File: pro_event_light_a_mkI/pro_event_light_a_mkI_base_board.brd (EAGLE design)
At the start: 68.9 x 76.6 mm, 85 parts, among them K1 62201021121, SW1 ALPS_EC11D

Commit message: modelled all four IL4001 PMICs
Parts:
- moved PMIC5:U1 276.1 mm to (59.9, 11.9), turned to 90 degrees
- moved PMIC5:R14 273.4 mm to (59.2, 9.78)
- moved PMIC5:PMIC1 269.8 mm to (56.8, 13.2), turned to 270 degrees
- moved PMIC5:L2 267.0 mm to (63.9, 11.8), turned to 180 degrees
- moved PMIC5:DZ1 262.9 mm to (61.0, 15.7), turned to 270 degrees
- moved PMIC5:C8 257.6 mm to (56.0, 15.7), turned to 180 degrees
- moved PMIC4:U1 248.0 mm to (42.8, 20.8), turned to 90 degrees
- moved PMIC4:R14 245.0 mm to (41.7, 18.0)
- moved PMIC4:PMIC1 242.1 mm to (39.4, 22.1), turned to 270 degrees
- moved PMIC3:U1 239.2 mm to (59.6, 26.8), turned to 90 degrees
- moved PMIC4:L2 238.3 mm to (47.0, 20.3), turned to 180 degrees
- moved PMIC3:R14 236.6 mm to (58.5, 24.5)
- moved PMIC4:DZ1 235.3 mm to (43.2, 24.8), turned to 270 degrees
- moved PMIC3:PMIC1 233.1 mm to (55.9, 28.2), turned to 270 degrees
- moved PMIC3:L2 230.5 mm to (64.0, 27.2), turned to 180 degrees
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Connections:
- removed net PMIC3:PMIC_IL4001_S24V: PMIC3:C8.2, PMIC3:DZ1.C, PMIC3:PMIC1.1
- removed net PMIC4:PMIC_IL4001_GND: PMIC4:C8.1, PMIC4:PMIC1.2, PMIC4:PMIC1.5, PMIC4:R14.1, PMIC4:U1.2
- net GND_MCU: now also PMIC4:C8.1, PMIC4:PMIC1.2, PMIC4:PMIC1.5, PMIC4:R14.1, PMIC4:U1.2
- net SUPPLY_24V: now also PMIC3:C8.2, PMIC3:DZ1.C, PMIC3:PMIC1.1
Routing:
- net PMIC4:N$2: track 0.00 -> 5.44 mm
- net PMIC3:N$2: track 0.00 -> 5.05 mm
- net PMIC5:N$2: track 0.00 -> 4.65 mm
- added copper zone on layer 1, net PMIC3:N$29
- added copper zone on layer 1, net PMIC4:N$29
- added copper zone on layer 1, net PMIC5:N$29

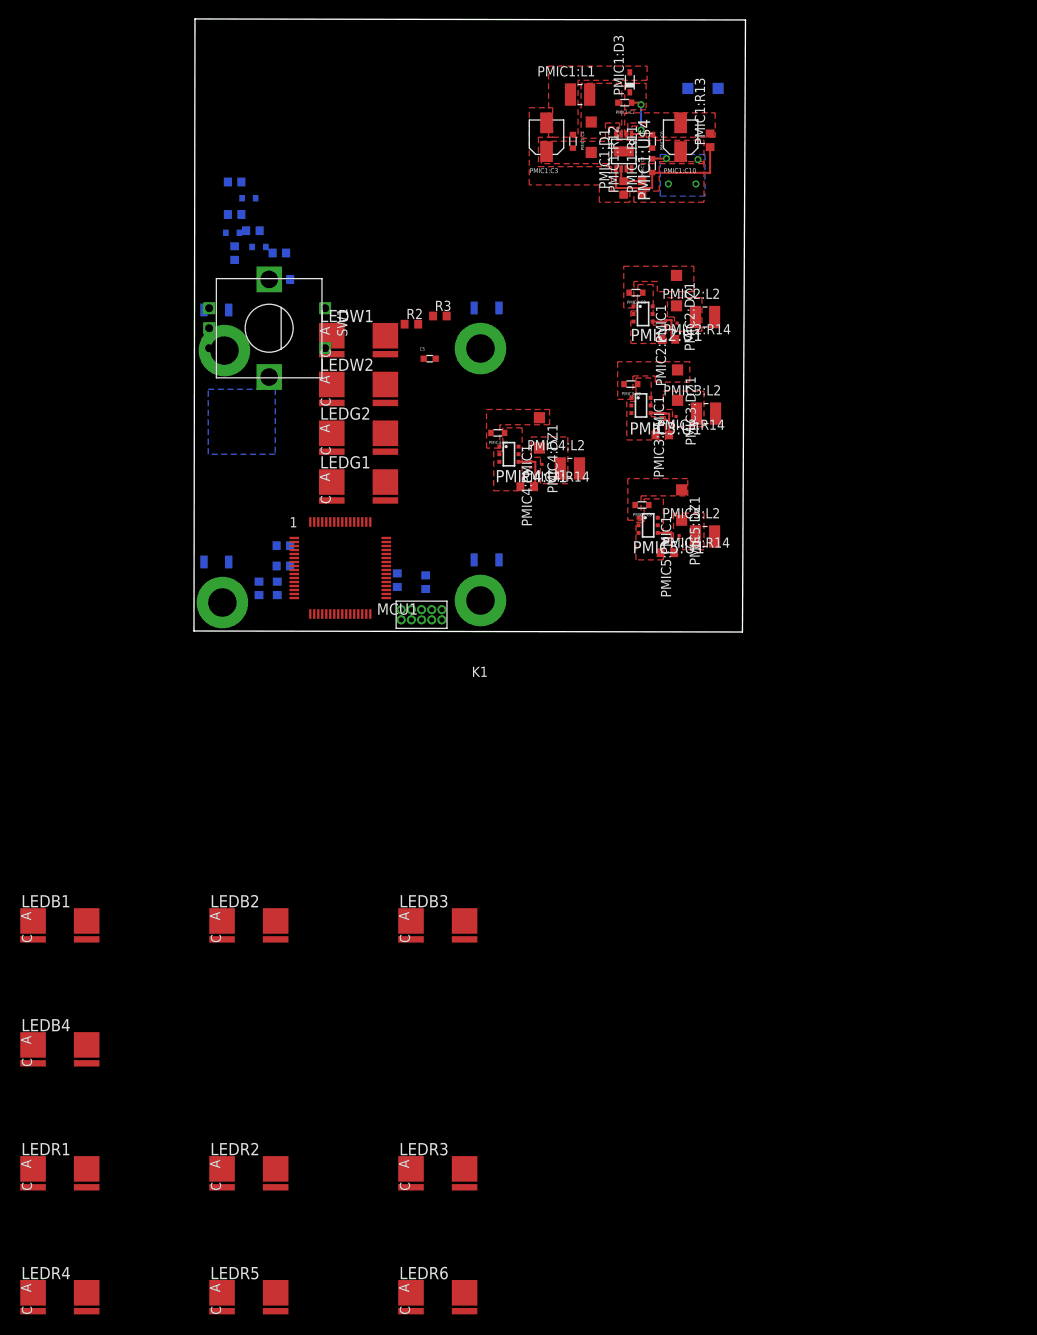
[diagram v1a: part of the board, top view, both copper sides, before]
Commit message: layout for all 4 IL4001
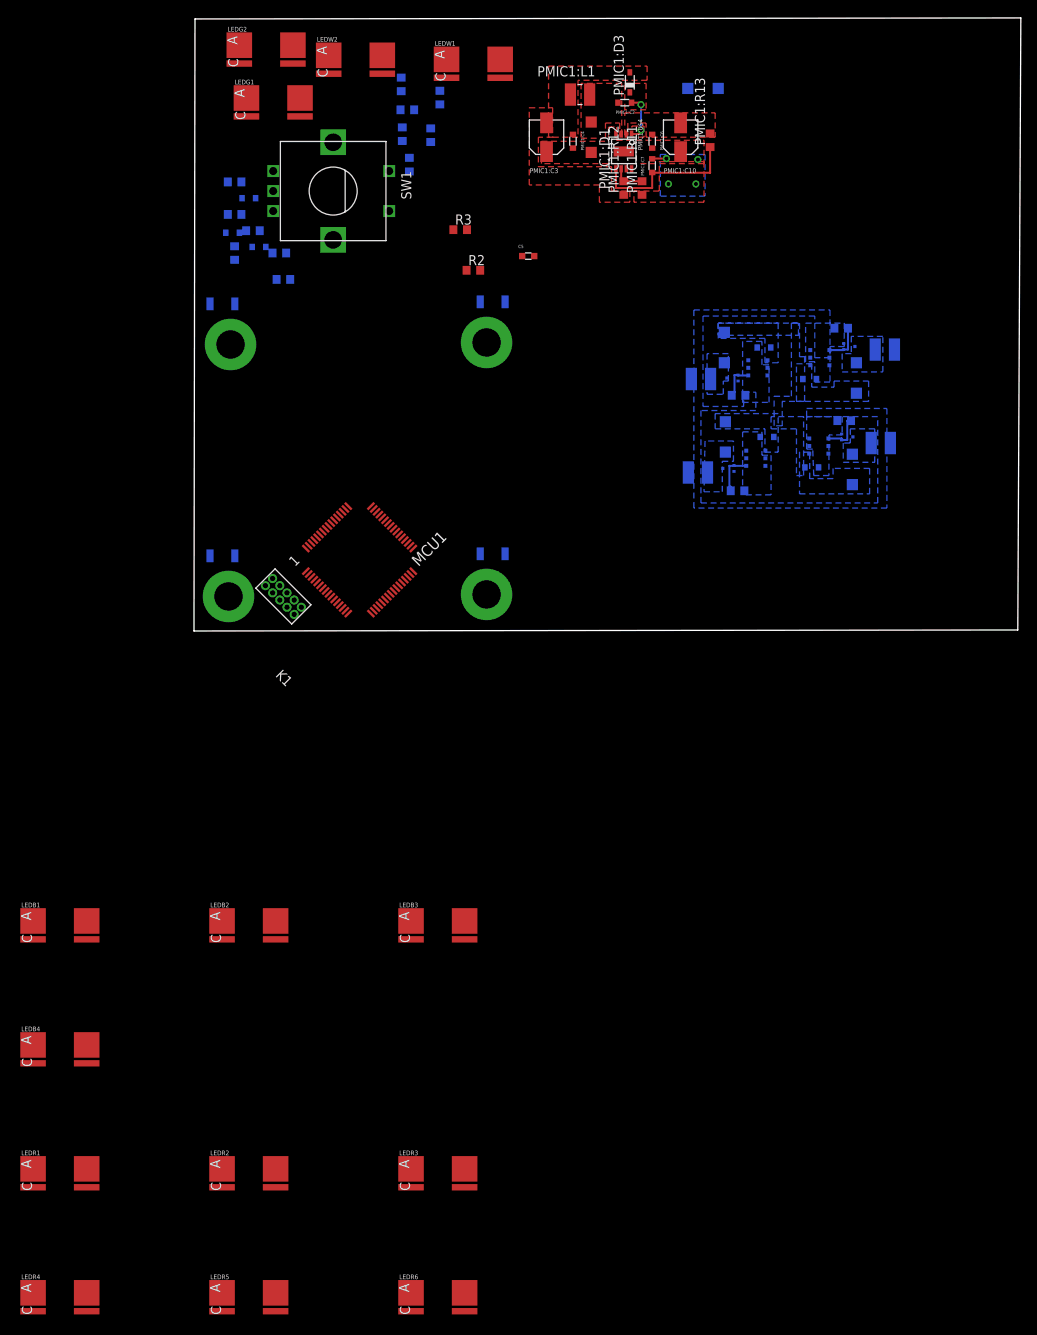
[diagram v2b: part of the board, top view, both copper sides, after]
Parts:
- moved R8 65.4 mm to (30.7, 66.7)
- moved R9 64.9 mm to (25.9, 68.3)
- moved R7 56.9 mm to (29.6, 62.0), turned to 90 degrees
- moved R10 56.6 mm to (26.7, 65.2)
- moved R36 55.8 mm to (26.0, 62.1)
- moved R35 52.2 mm to (26.9, 58.3)
- moved LEDG2 49.9 mm to (9.02, 71.6)
- moved LEDG1 49.2 mm to (9.91, 65.0)
- moved LEDW2 41.1 mm to (20.2, 70.4)
- moved LEDW1 37.4 mm to (34.9, 69.8)
- moved PMIC4:C8 33.7 mm to (71.6, 24.3), flipped to the bottom
- moved PMIC2:DZ1 31.3 mm to (82.3, 20.2), flipped to the bottom, turned to 90 degrees
- moved PMIC2:C8 31.0 mm to (77.2, 20.4), flipped to the bottom, turned to 0 degrees
- moved PMIC4:PMIC1 30.9 mm to (70.2, 21.6), flipped to the bottom
- moved PMIC2:PMIC1 27.5 mm to (78.1, 23.1), flipped to the bottom, turned to 90 degrees
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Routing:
- added copper zone on layer 16, net PMIC2:N$29
- added copper zone on layer 16, net PMIC3:N$29
- added copper zone on layer 16, net PMIC4:N$29
- added copper zone on layer 16, net PMIC5:N$29
- added copper zone on layer 16, net SUPPLY_24V
- removed copper zone on layer 1, net PMIC2:N$29
- removed copper zone on layer 1, net PMIC3:N$29
- removed copper zone on layer 1, net PMIC4:N$29
- removed copper zone on layer 1, net PMIC5:N$29
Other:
- board size 68.9 x 76.6 mm -> 103.4 x 76.6 mm

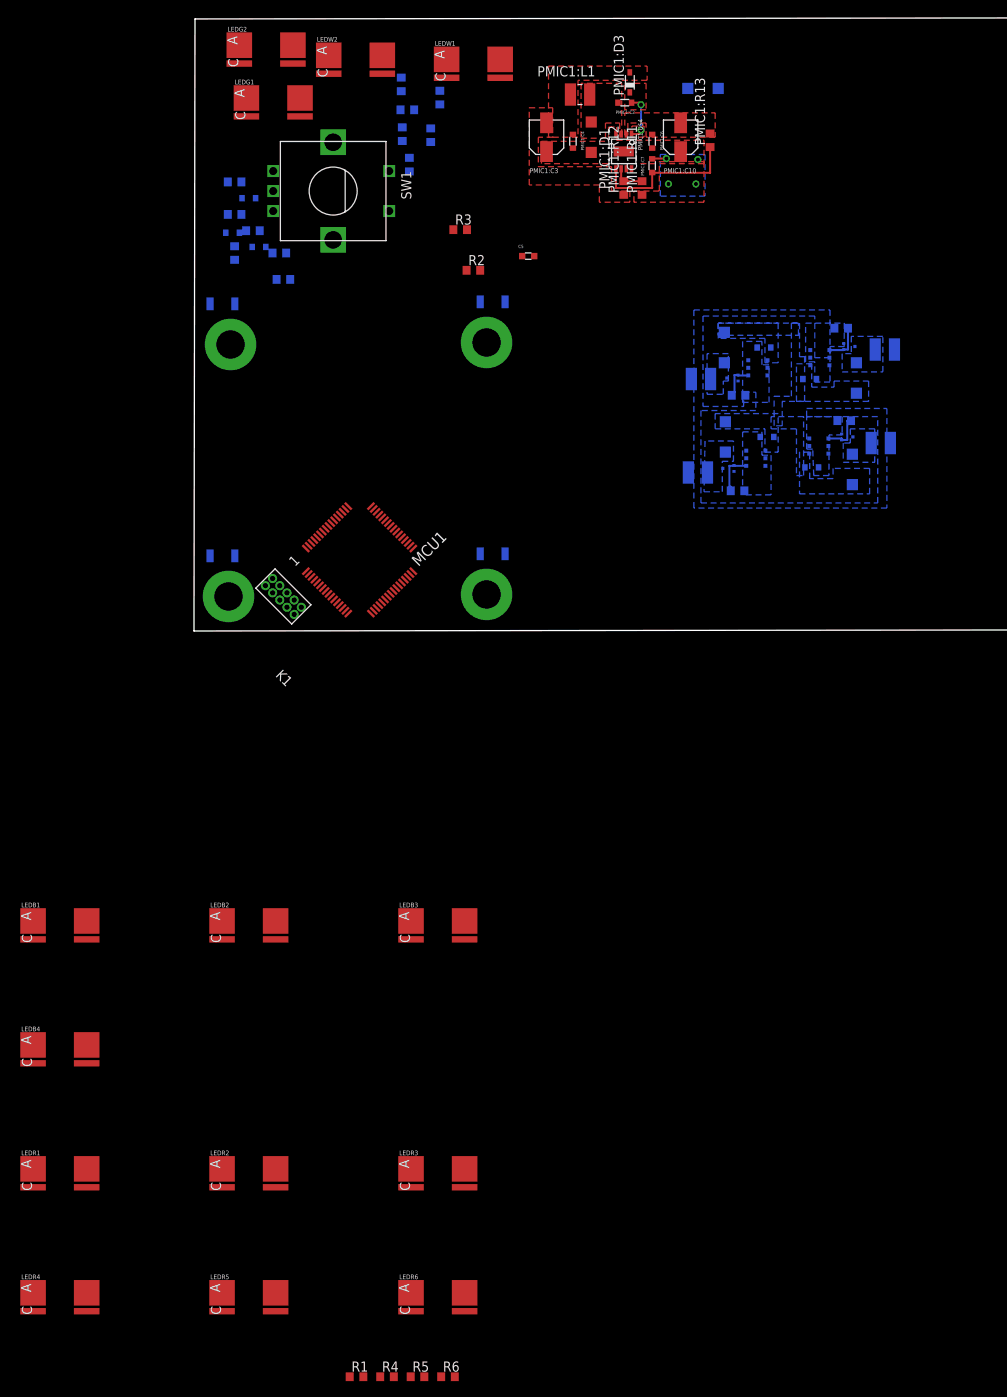
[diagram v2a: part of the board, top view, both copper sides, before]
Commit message: first layout for LEDs
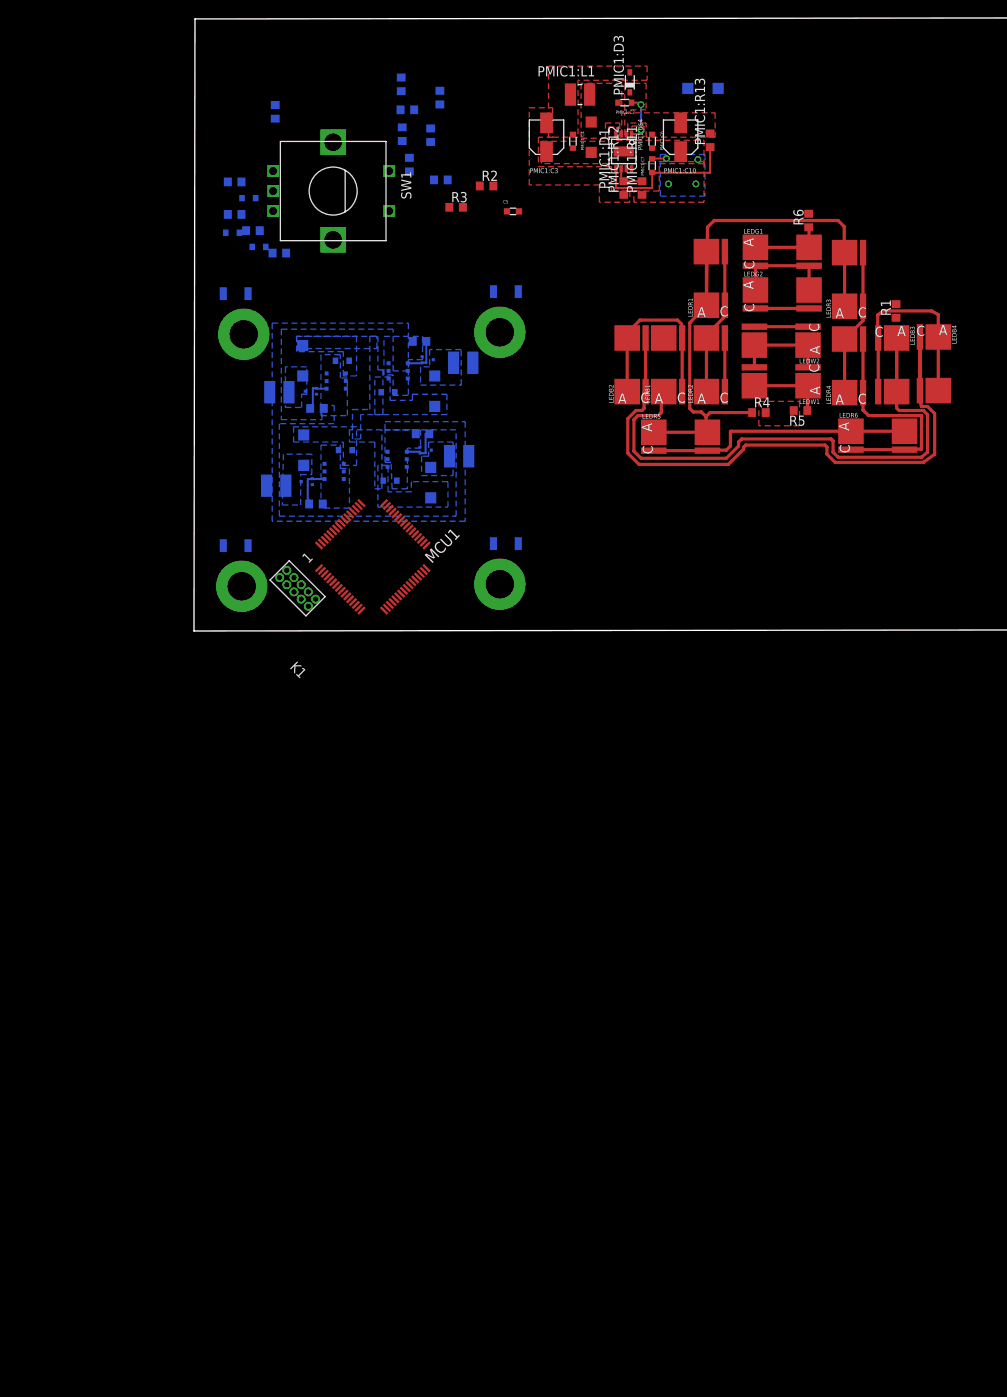
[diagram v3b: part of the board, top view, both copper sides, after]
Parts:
- moved LEDR4 154.1 mm to (82.9, 33.1), turned to 90 degrees
- moved R6 151.4 mm to (76.8, 51.3), turned to 90 degrees
- moved R1 149.3 mm to (87.8, 40.0), turned to 90 degrees
- moved LEDR1 139.8 mm to (65.7, 44.1), turned to 90 degrees
- moved LEDB4 138.7 mm to (91.4, 33.4), turned to 270 degrees
- moved R5 129.9 mm to (75.8, 27.6), turned to 180 degrees
- moved R4 129.2 mm to (70.6, 27.3)
- moved LEDR3 124.4 mm to (82.9, 43.9), turned to 90 degrees
- moved LEDR6 120.9 mm to (85.5, 23.4)
- moved LEDR5 120.4 mm to (60.8, 23.2)
- moved LEDR2 117.8 mm to (65.7, 33.3), turned to 90 degrees
- moved LEDB1 104.9 mm to (60.3, 33.3), turned to 90 degrees
- moved LEDB3 90.4 mm to (86.2, 33.3), turned to 270 degrees
- moved LEDB2 86.3 mm to (55.8, 33.3), turned to 90 degrees
- moved LEDG2 71.4 mm to (73.5, 41.0)
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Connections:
- net DRIVER_LEDG: now also LEDG2.3, LEDG2.4; no longer LEDG1.3, LEDG1.4
- net N$3: now also LEDG1.3, LEDG1.4, LEDG2.1, LEDG2.2; no longer LEDG1.1, LEDG1.2, LEDG2.3, LEDG2.4
- net VSENSE_LEDG: now also LEDG1.1, LEDG1.2; no longer LEDG2.1, LEDG2.2
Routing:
- net DRIVER_LEDB: track 0.00 -> 80.2 mm
- net VSENSE_LEDR: track 0.00 -> 76.6 mm
- net VSENSE_LEDB: track 0.00 -> 75.2 mm
- net DRIVER_LEDR: track 0.00 -> 36.5 mm
- net N$14: track 0.00 -> 33.4 mm
- net N$6: track 0.00 -> 29.6 mm
- net N$4: track 0.00 -> 24.8 mm
- net N$12: track 0.00 -> 18.4 mm
- net N$7: track 0.00 -> 18.4 mm
- net N$3: track 0.00 -> 12.8 mm
- net N$25: track 0.00 -> 12.3 mm
- net VSENSE_LEDW: track 0.00 -> 9.80 mm
- net VSENSE_LEDG: track 0.00 -> 9.22 mm
- net DRIVER_LEDW: track 0.00 -> 6.70 mm
- net DRIVER_LEDG: track 0.00 -> 6.70 mm

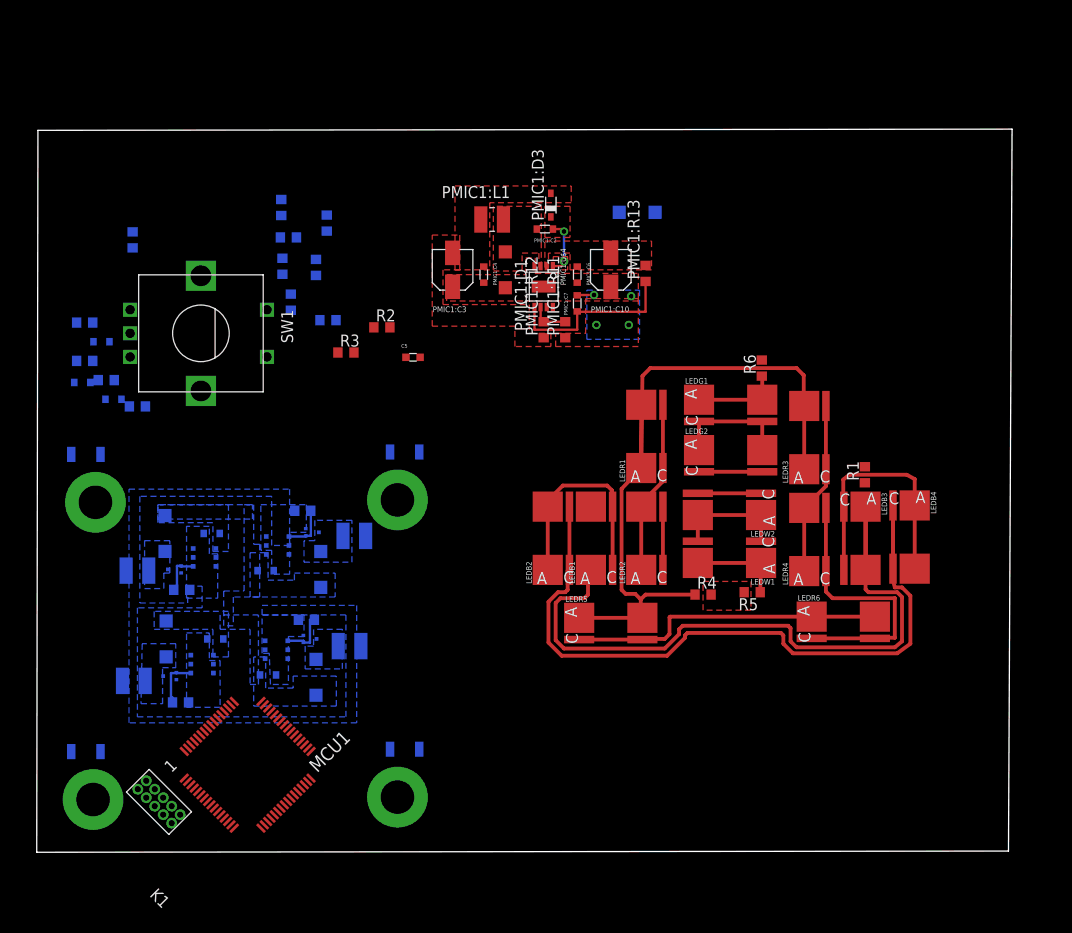
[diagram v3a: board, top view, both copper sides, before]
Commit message: cannot accomplished one board, hence split up into two boards
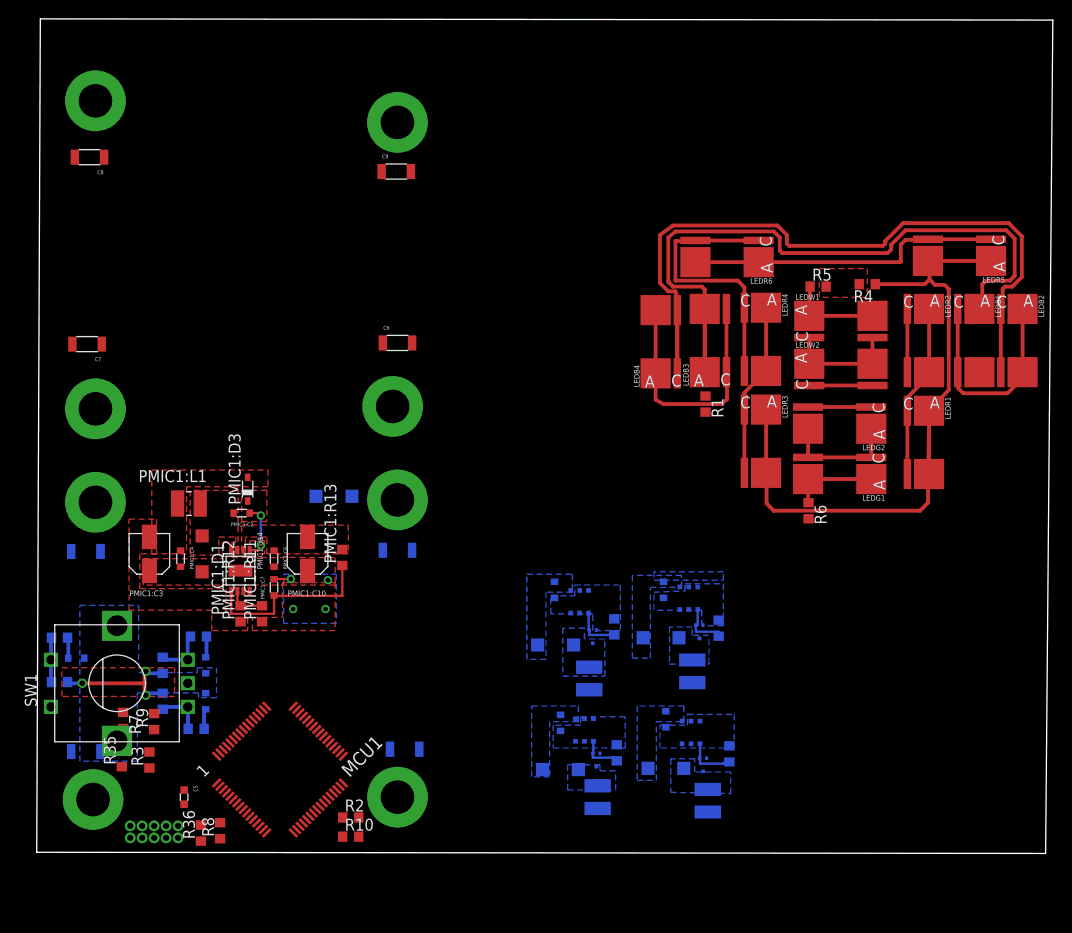
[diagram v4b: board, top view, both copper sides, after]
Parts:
- added C6, C7, C8, C9: 1uF, Eagle_Wurth_Elektronik_Passive_Capacitors_rev15a:WCAP-CSGP_1206
- added U$1, U$2, U$3, U$4: (no value), mod-eagle_library_standard_passive_parts:PCB_MOUNTING_HOLES_M3
- moved R8 65.4 mm to (19.4, 2.29), flipped to the top
- moved R10 63.8 mm to (33.3, 1.65), flipped to the top
- moved PMIC4:L2 62.1 mm to (71.1, 5.46), turned to 90 degrees
- moved R36 60.7 mm to (17.4, 2.03), flipped to the top
- moved PMIC4:R14 58.4 mm to (73.4, 10.4), turned to 270 degrees
- moved PMIC4:U1 57.3 mm to (70.6, 9.27), turned to 0 degrees
- moved R9 56.1 mm to (12.4, 13.8), flipped to the top
- moved LEDR5 55.2 mm to (97.8, 64.3), turned to 180 degrees
- moved PMIC4:DZ1 54.7 mm to (66.7, 8.89), turned to 180 degrees
- moved PMIC5:L2 54.4 mm to (59.4, 5.84), turned to 90 degrees
- moved C5 52.5 mm to (15.6, 5.84), turned to 270 degrees
- moved PMIC4:PMIC1 52.3 mm to (69.3, 12.7), turned to 180 degrees
- moved R7 52.2 mm to (9.14, 14.0), flipped to the top, turned to 270 degrees
- moved R2 52.0 mm to (33.3, 3.68)
- moved R35 51.6 mm to (9.02, 9.91), flipped to the top
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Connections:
- removed net N$13: C2.2, R14.2
- new net ENCODER_A: C2.2, MCU1.26, R14.2
- new net ENCODER_B: C3.2, MCU1.27, R15.1
- new net ENCODER_D: C4.2, MCU1.28, R16.1
- net GND_MCU: now also C2.1, C3.1, C4.1, C6.2, C7.2, C8.2, C9.2, SW1.C, SW1.D, SW1.GND1, SW1.GND2
- net LEDB: now also MCU1.15; no longer MCU1.35
- net LEDG: now also MCU1.14; no longer MCU1.36
- net LEDR: now also MCU1.16; no longer MCU1.34
- net LEDW: now also MCU1.17; no longer MCU1.33
- net N$10: now also C8.1, U$3.PIN1; no longer R11.2, R12.2, R13.2
- net N$11: now also C9.1, U$4.PIN1; no longer C3.2, R15.1
- net N$5: now also C6.1, U$2.PIN1; no longer C2.1, C3.1, C4.1, SW1.C, SW1.D, SW1.GND1, SW1.GND2
- net N$8: now also C7.1, U$1.PIN1; no longer C4.2, R16.1
- net S3V3_MCU_VDD: now also R11.2, R12.2, R13.2
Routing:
- net S3V3_MCU_VDD: track 0.00 -> 15.1 mm, vias 0 -> 3
- net N$2: track 0.00 -> 5.57 mm
- net N$1: track 0.00 -> 5.14 mm
- net N$16: track 0.00 -> 4.76 mm
- net ENCODER_B: track 0.00 -> 2.29 mm
- net ENCODER_A: track 0.00 -> 2.24 mm
- net ENCODER_D: track 0.00 -> 2.24 mm
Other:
- board size 103.4 x 76.6 mm -> 107.7 x 88.4 mm
